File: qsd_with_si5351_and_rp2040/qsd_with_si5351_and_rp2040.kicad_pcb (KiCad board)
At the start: 2 copper layers, 100 x 50 mm, 113 parts, among them J1 Conn_Coaxial, J101 Conn_01x02, J102 Conn_01x02, J103 Conn_01x04, J104 Conn_01x04, J105 Conn_02x14_Odd_Even, J106 Conn_01x03, J2 USB_C_Receptacle_USB2.0, J201 Conn_01x02, J202 Conn_01x03, J203 Conn_01x03, J3 Conn_01x04, U1 CX2047LNL, U101 RP2040, U102 W25Q128JVS, U103 MS5351M, U2 SN74CBTLV3253PW, U201 AP1117-33, U3 LM4562, U4 LM4562, U5 LM4562, U666 Pico, Y101 403C35D12M00000, Y102 MCSJK-7U-27.00-10-10-60-B-10

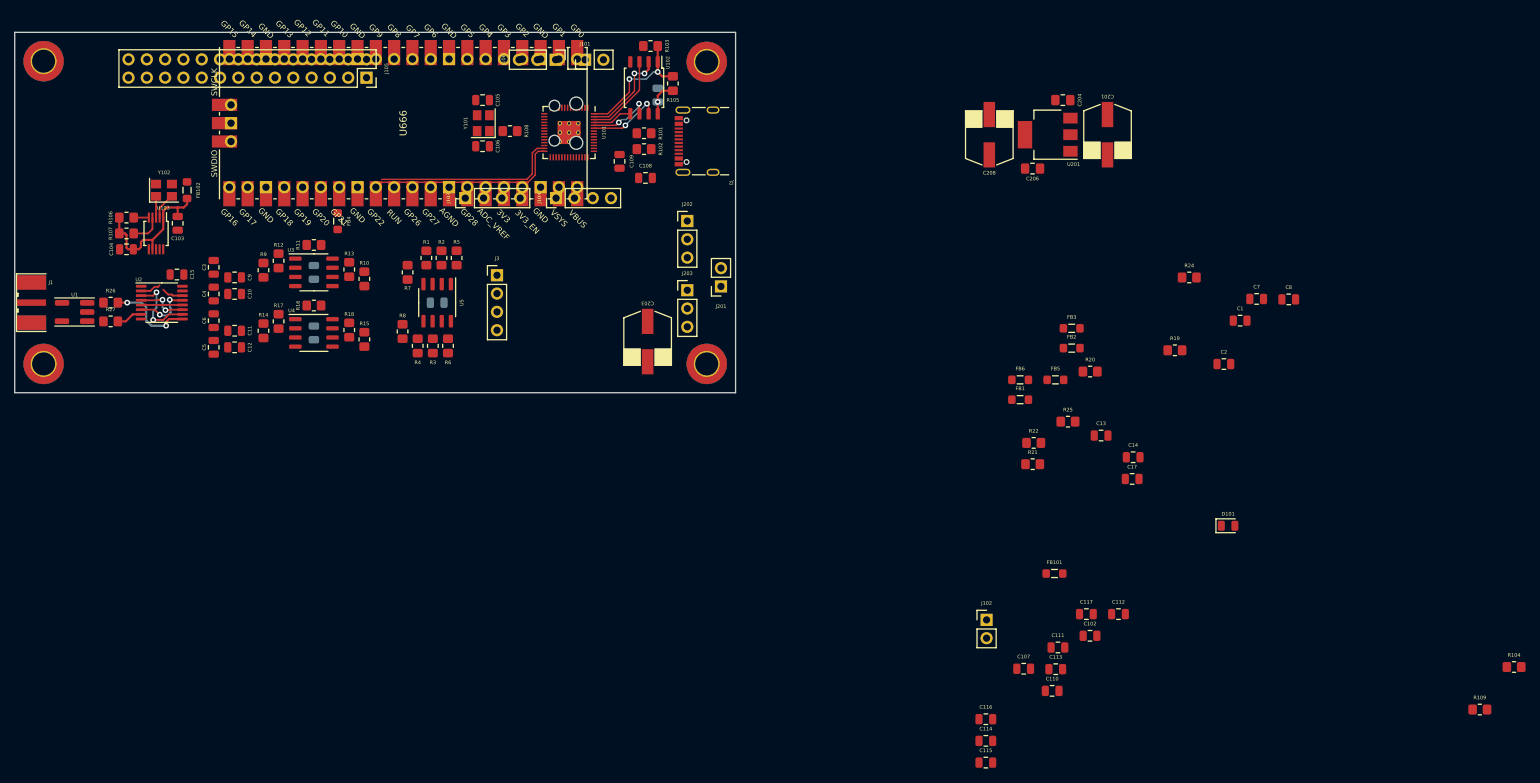
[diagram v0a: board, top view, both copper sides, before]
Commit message: version with stackable connector
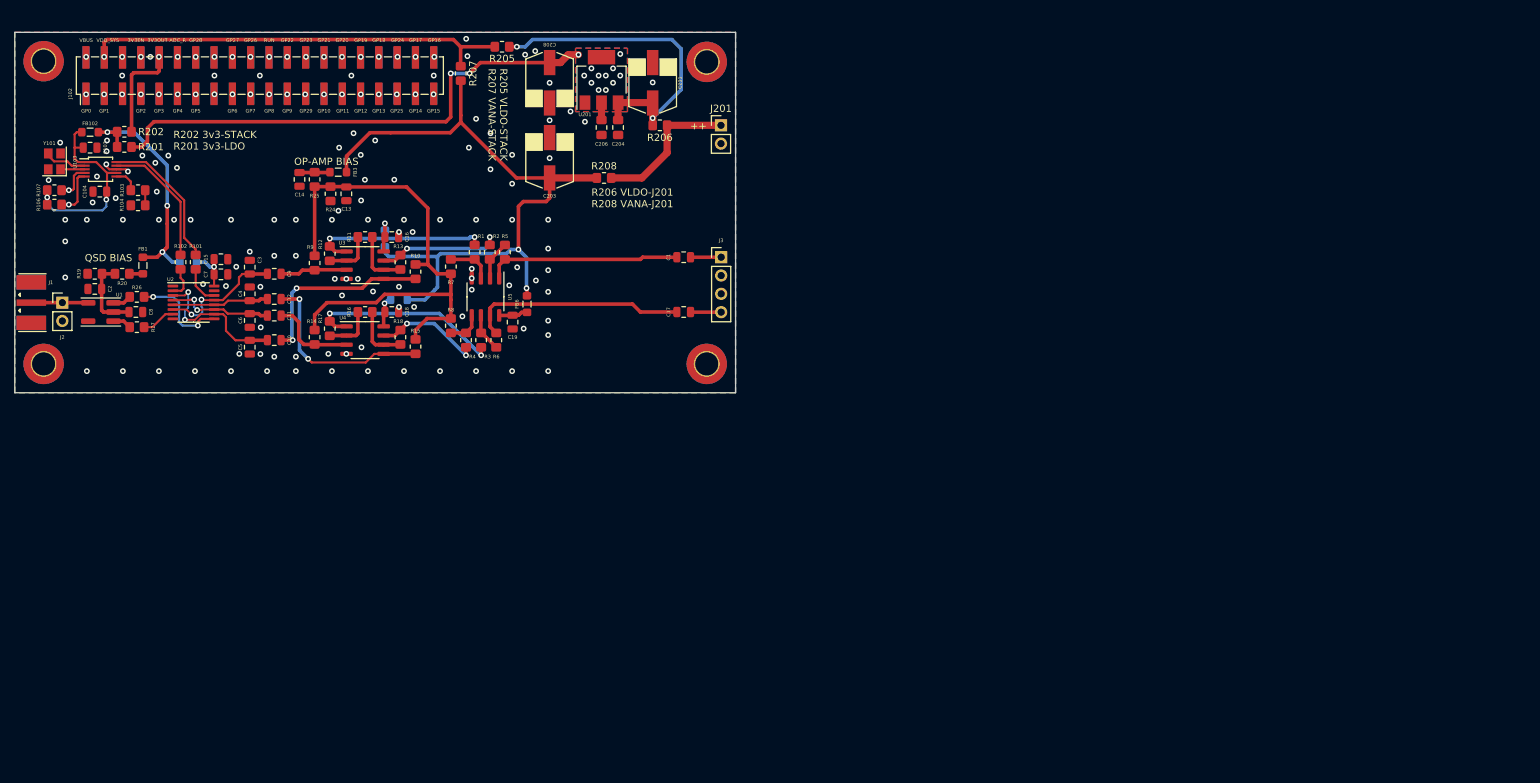
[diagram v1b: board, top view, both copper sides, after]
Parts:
- removed C101, C107, C108, C111, C112, C113, C114, C115, C116: 100n, Capacitor_SMD:C_0805_2012Metric
- removed C102: 1n, Capacitor_SMD:C_0805_2012Metric
- removed C105, C106: 27p, Capacitor_SMD:C_0805_2012Metric
- removed C109, C110, C117: 1u, Capacitor_SMD:C_0805_2012Metric
- removed D101: LED_RED, Diode_SMD:D_0805_2012Metric
- removed FB101: 1000, Inductor_SMD:L_0805_2012Metric_Pad1.05x1.20mm_HandSolder
- removed J103, J104: Conn_01x04, Connector_PinHeader_2.54mm:PinHeader_1x04_P2.54mm_Vertical
- removed J105: Conn_02x14_Odd_Even, Connector_PinSocket_2.54mm:PinSocket_2x14_P2.54mm_Vertical
- removed J106, J202, J203: Conn_01x03, Connector_PinHeader_2.54mm:PinHeader_1x03_P2.54mm_Vertical
- removed R105: DNP, Resistor_SMD:R_0805_2012Metric_Pad1.20x1.40mm_HandSolder
- removed R108, R109: 1K, Resistor_SMD:R_0805_2012Metric_Pad1.20x1.40mm_HandSolder
- removed R21, R22: 5.1k, Resistor_SMD:R_0805_2012Metric_Pad1.20x1.40mm_HandSolder
- removed U101: RP2040, MCU_RaspberryPi_and_Boards:RP2040-QFN-56
- removed U102: W25Q128JVS, Package_SO:SOIC-8_5.23x5.23mm_P1.27mm
- removed U666: Pico, MCU_RaspberryPi_and_Boards:RPi_Pico_SMD_TH
- removed Y102: MCSJK-7U-27.00-10-10-60-B-10, Crystal:Crystal_SMD_3225-4Pin_3.2x2.5mm
- added R201: 0, Resistor_SMD:R_0805_2012Metric_Pad1.20x1.40mm_HandSolder, F.Cu at (40.2, 38.9)
- added R202: 0, Resistor_SMD:R_0805_2012Metric_Pad1.20x1.40mm_HandSolder, F.Cu at (40.2, 36.8)
- added R205: 0, Resistor_SMD:R_0805_2012Metric_Pad1.20x1.40mm_HandSolder, F.Cu at (92.6, 25.0)
- added R206: 0, Resistor_SMD:R_0805_2012Metric_Pad1.20x1.40mm_HandSolder, F.Cu at (114.5, 35.9)
- added R207: 0, Resistor_SMD:R_0805_2012Metric_Pad1.20x1.40mm_HandSolder, F.Cu at (86.9, 28.7)
- added R208: 0, Resistor_SMD:R_0805_2012Metric_Pad1.20x1.40mm_HandSolder, F.Cu at (106.8, 43.2)
- C16, C18, C19: moved to F.Cu
- FB2, FB4, FB5: moved to B.Cu
- J101: value Conn_01x02 -> SSM-120-F-DV; footprint Connector_PinHeader_2.54mm:PinHeader_1x02_P2.54mm_Vertical -> Connector_PinSocket_2.54mm:PinSocket_2x20_P2.54mm_Vertical_SMD; moved to B.Cu
- J102: value Conn_01x02 -> M20-8762042; footprint Connector_PinHeader_2.54mm:PinHeader_1x02_P2.54mm_Vertical -> Connector_PinHeader_2.54mm:PinHeader_2x20_P2.54mm_Vertical_SMD
- J2: value USB_C_Receptacle_USB2.0 -> Conn_01x02; footprint Connector_USB:USB_C_Receptacle_GCT_USB4105-xx-A_16P_TopMnt_Horizontal -> Connector_PinHeader_2.54mm:PinHeader_1x02_P2.54mm_Vertical
- J201: footprint Connector_PinSocket_2.54mm:PinSocket_1x02_P2.54mm_Vertical -> Connector_PinHeader_2.54mm:PinHeader_1x02_P2.54mm_Vertical
- R101, R102: value 27.4 -> 0
- R103: value 1K -> 0
- R104: value 10k -> 0
- Y101: value 403C35D12M00000 -> MCSJK-7U-27.00-10-10-60-B-10
- moved R104 201.4 mm to (42.1, 47.0), turned to 180 degrees
- moved C8 159.9 mm to (41.8, 61.8)
- moved C2 157.0 mm to (36.1, 58.6), turned to 180 degrees
- moved R19 150.2 mm to (36.1, 56.5), turned to 180 degrees
- moved C7 143.7 mm to (53.6, 56.6)
- moved R20 135.0 mm to (39.9, 56.5), turned to 180 degrees
- moved J102 126.0 mm to (59.0, 29.0), turned to 90 degrees
- moved FB2 123.2 mm to (49.0, 54.9)
- moved FB1 123.1 mm to (42.8, 55.4), turned to -90 degrees
- moved C14 121.9 mm to (64.5, 43.4), turned to -90 degrees
- moved R24 119.7 mm to (68.8, 45.4), turned to -90 degrees
- moved C13 110.0 mm to (71.0, 45.4), turned to -90 degrees
- moved R25 109.8 mm to (66.6, 43.4), turned to -90 degrees
- moved FB3 104.0 mm to (69.9, 42.4), turned to 180 degrees
- moved J2 92.0 mm to (31.6, 60.5), turned to 0 degrees
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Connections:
- net /control_board/GPIO4 renamed /control_board/I2C0_SDA
- net /control_board/GPIO5 renamed /control_board/I2C0_SCL
- C206 pad 1: VCC_3V3 -> Net-(C206-Pad1)
- C208 pad 1: VCC_3V3 -> Net-(C206-Pad1)
- FB1 pad 1: VCC_3V3 -> VCC_3V3_MIX
- FB102 pad 1: VCC_3V3 -> VCC_3V3_MIX
- FB2 pad 1: VCC_3V3 -> VCC_3V3_MIX
- J101 pad 1: Net-(J101-Pad1) -> GPIO0
- J101 pad 2: GND -> VBUS
- J102 pad 1: Net-(U101-Pad26) -> GPIO0
- J102 pad 2: GND -> VBUS
- R101 pad 1: Net-(R101-Pad1) -> Net-(U103-Pad10)
- R101 pad 2: /USB_D+ -> QSD_CLK_S0
- R102 pad 2: /USB_D- -> QSD_CLK_S1
- R103 pad 1: Net-(J101-Pad1) -> Net-(R103-Pad1)
- R103 pad 2: /control_board/QSPI_SS -> /control_board/CLK_2
- R104 pad 1: VCC_3V3 -> /control_board/CLK_2
- R104 pad 2: Net-(U101-Pad26) -> GND
- U103 pad 10: QSD_CLK_S0 -> Net-(U103-Pad10)
- U103 pad 6: /control_board/CLK_2 -> Net-(R103-Pad1)
- U103 pad 9: QSD_CLK_S1 -> Net-(R102-Pad1)
- U201 pad 2: VCC_3V3 -> Net-(C206-Pad1)
- Y101 pad 1: Net-(Y101-Pad1) -> Net-(U103-Pad3)
- Y101 pad 2: Net-(U101-Pad20) -> GND
- Y101 pad 3: (no net) -> Net-(U103-Pad2)
- Y101 pad 4: (no net) -> GND
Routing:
- net VCC_ANALOG: track 0.00 -> 97.5 mm, vias 0 -> 2
- net /OPAMP_BIAS: track 0.00 -> 75.0 mm
- net Net-(C206-Pad1): track 0.00 -> 74.3 mm, vias 0 -> 14
- net VDD_SYS: track 0.00 -> 59.6 mm, vias 0 -> 1
- net Net-(R206-Pad1): track 0.00 -> 46.4 mm, vias 0 -> 2
- net VCC_3V3_MIX: track 0.00 -> 33.2 mm, vias 0 -> 3
- net Net-(C17-Pad1): track 0.00 -> 30.4 mm
- net /270: track 0.00 -> 28.2 mm, vias 0 -> 2
- net Net-(C1-Pad1): track 0.00 -> 26.9 mm
- net Net-(C12-Pad2): track 0.00 -> 26.8 mm, vias 0 -> 2
- net /control_board/GPIO17: track 26.6 -> 0.00 mm
- net Net-(C10-Pad2): track 0.00 -> 26.2 mm, vias 0 -> 2
- net /control_board/GPIO16: track 26.0 -> 0.00 mm
- net /0: track 0.00 -> 25.0 mm, vias 0 -> 2
- net /power/ANALOG_AUX: track 0.00 -> 20.5 mm
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- added copper zone on B.Cu, net GND
- added copper zone on F.Cu, net GND
- added copper zone on B.Cu, net Net-(C206-Pad1)
- added copper zone on F.Cu, net Net-(C206-Pad1)
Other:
- board text added: "++"
- board text added: "3V3EN"
- board text added: "3V3OUT"
- board text added: "ADC_R"
- board text added: "CENTERED AT : X34 Y6 FROM TOP LEFT CORNER"
- board text added: "GP0"
- board text added: "GP1"
- board text added: "GP10"
- board text added: "GP11"
- board text added: "GP12"
- board text added: "GP13"
- board text added: "GP14"
- board text added: "GP15"
- board text added: "GP16"
- board text added: "GP17"
- board text added: "GP18"
- board text added: "GP19"
- board text added: "GP2"
- board text added: "GP20"
- board text added: "GP21"
- board text added: "GP22"
- board text added: "GP23"
- board text added: "GP24"
- board text added: "GP25"
- board text added: "GP26"
- board text added: "GP27"
- board text added: "GP28"
- board text added: "GP29"
- board text added: "GP3"
- board text added: "GP4"
- board text added: "GP5"
- board text added: "GP6"
- board text added: "GP7"
- board text added: "GP8"
- board text added: "GP9"
- board text added: "OP-AMP BIAS"
- board text added: "QSD BIAS"
- board text added: "R202 3v3-STACK R201 3v3-LDO"
- board text added: "R205 VLDO-STACK R207 VANA-STACK"
- board text added: "R206 VLDO-J201 R208 VANA-J201"
- board text added: "RUN"
- board text added: "VBUS"
- board text added: "VDD_SYS"

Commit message: ready for production
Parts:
- FB2: moved to F.Cu
- moved C17 18.1 mm to (99.7, 60.7)
- moved C1 18.1 mm to (99.7, 54.5)
- moved FB2 5.29 mm to (53.8, 52.5), turned to 180 degrees
- moved FB4 1.40 mm to (76.3, 53.0)
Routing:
- net VCC_3V3_MIX: track 33.2 -> 61.5 mm
- net Net-(C17-Pad1): track 30.4 -> 11.8 mm
- net /OUT_Q: track 4.26 -> 22.8 mm
- net Net-(C1-Pad1): track 26.9 -> 8.70 mm
- net /OUT_I: track 4.25 -> 22.5 mm
- net Net-(C12-Pad2): track 26.8 -> 24.7 mm
- net Net-(C16-Pad1): track 4.96 -> 2.95 mm
- net Net-(R106-Pad1): track 28.7 -> 29.8 mm
- net VCC_ANALOG: track 97.5 -> 96.5 mm
- net /0: track 25.0 -> 25.9 mm
- net Net-(C15-Pad1): track 6.45 -> 5.66 mm, vias 1 -> 0
- net Net-(C206-Pad1): vias 14 -> 9
- net GND: vias 118 -> 115
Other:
- board text added: "GND"
- board text added: "OUT I"
- board text added: "OUT Q"
